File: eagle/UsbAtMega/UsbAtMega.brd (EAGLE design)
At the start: 33.5 x 28.6 mm, 16 parts, among them U1 ATMEGA328P_PDIP, U2 FT232RLSSOP

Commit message: tweaks
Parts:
- added JP1: (no value), SparkFun-Connectors:1X06
- moved Y1 63.5 mm to (60.5, 8.45)
- moved C5 61.1 mm to (52.6, 8.12)
- moved U1 44.8 mm to (55.6, 18.5)
- moved R11 41.0 mm to (38.4, 5.85), turned to 270 degrees
- moved C4 38.9 mm to (32.8, 8.78)
- moved R3 13.9 mm to (30.2, 20.5)
- moved RX 6.70 mm to (24.4, 26.0), turned to 90 degrees
- moved TX 5.81 mm to (16.6, 26.0), turned to 90 degrees
- moved R2 4.97 mm to (11.1, 23.7)
- moved R1 4.65 mm to (7.15, 23.7)
- moved U2 3.91 mm to (19.8, 13.3)
- moved PWR 3.71 mm to (28.6, 5.20), turned to 90 degrees
- moved C2 3.71 mm to (13.3, 5.53), turned to 270 degrees
- moved C3 3.71 mm to (21.1, 3.25)
- moved USB 2.62 mm to (2.60, 17.2)
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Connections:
- removed net 5V1: C5.1
- new net N$10: JP1.5, U1.27
- new net N$11: JP1.4, U1.26
- new net N$12: JP1.3, U1.25
- new net N$18: JP1.2, U1.24
- new net N$19: JP1.1, U1.23
- new net N$9: JP1.6, U1.28
- net 5V: now also C5.1
- net N$1: now also U1.1
- net N$7: now also U1.9
- net N$8: now also U1.10
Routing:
- net 5V: track 77.7 -> 0.00 mm, vias 1 -> 0
- net GND: track 76.2 -> 0.00 mm, vias 1 -> 0
- net 3.3V: track 33.2 -> 0.00 mm, vias 1 -> 0
- net N$13: track 19.8 -> 0.00 mm, vias 1 -> 0
- net N$17: track 17.9 -> 0.00 mm, vias 1 -> 0
- net N$2: track 17.7 -> 0.00 mm
- net N$16: track 15.7 -> 0.00 mm
- net N$14: track 14.9 -> 0.00 mm, vias 1 -> 0
- net N$15: track 13.7 -> 0.00 mm
- net N$3: track 10.5 -> 0.00 mm
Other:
- board size 33.5 x 28.6 mm -> 75.4 x 29.9 mm
- board text removed: "3.3V"
- board text removed: "5V"
- board text removed: "MARKY'S HOUSE"
- board text removed: "USB THANG"

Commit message: Start Manual routing
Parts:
- moved USB 0.32 mm to (2.60, 17.6)
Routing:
- net GND: track 0.00 -> 50.8 mm, vias 0 -> 6
- net 5V: track 0.00 -> 37.3 mm, vias 0 -> 1
- net N$2: track 0.00 -> 21.0 mm, vias 0 -> 1
- net 3.3V: track 0.00 -> 17.6 mm, vias 0 -> 1
- net N$13: track 0.00 -> 16.6 mm, vias 0 -> 1
- net N$3: track 0.00 -> 13.4 mm
- net N$14: track 0.00 -> 12.0 mm, vias 0 -> 1
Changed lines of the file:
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@@
 </autorouter>
 <elements>
-<element name="USB" library="SparkFun-Connectors" package="1X04_LOCK" value="" x="2.6" y="17.225" smashed="yes" rot="R270">
-<attribute name="NAME" x="0.8538" y="18.8962" size="1.27" layer="25" ratio="10"/>
-<attribute name="VALUE" x="-0.575" y="18.495" size="1.27" layer="27" rot="R270"/>
+<element name="USB" library="SparkFun-Connectors" package="1X04_LOCK" value="" x="2.6" y="17.55" smashed="yes" rot="R270">
+<attribute name="NAME" x="0.8538" y="19.2212" size="1.27" layer="25" ratio="10"/>
+<attribute name="VALUE" x="-0.575" y="18.82" size="1.27" layer="27" rot="R270"/>
 </element>
 <element name="U2" library="SparkFun-DigitalIC" package="SSOP28DB" value="FT232RLSSOP" x="19.825" y="13.325" smashed="yes" rot="R90">
 <attribute name="PROD_ID" value="IC-00870" x="19.825" y="13.325" size="1.778" layer="27" rot="R90" display="off"/>
-<attribute name="NAME" x="17.905" y="8.54" size="0.4064" layer="25" rot="R90"/>
+<attribute name="NAME" x="18.23" y="8.865" size="0.4064" layer="25" rot="R90"/>
 </element>
 <element name="C1" library="SparkFun-Capacitors" package="CAP-PTH-SMALLEZ" value="0.1uF" x="7.15" y="4.225" smashed="yes" rot="R90">
@@
 <contactref element="USB" pad="4"/>
 <contactref element="U2" pad="16"/>
-<wire x1="2.473" y1="9.605" x2="16.169" y2="16.9" width="0" layer="19" extent="1-1"/>
+<wire x1="16.169" y1="16.9" x2="5.85" y2="16.9" width="0.4064" layer="1"/>
+<wire x1="5.85" y1="16.9" x2="5.85" y2="16.25" width="0.4064" layer="1"/>
+<wire x1="5.85" y1="16.25" x2="4.55" y2="16.25" width="0.4064" layer="1"/>
+<via x="4.55" y="16.25" extent="1-16" drill="0.6"/>
+<wire x1="4.55" y1="16.25" x2="4.55" y2="9.75" width="0.4064" layer="16"/>
+<wire x1="4.55" y1="9.75" x2="2.473" y2="9.75" width="0.4064" layer="16"/>
+<wire x1="2.473" y1="9.75" x2="2.473" y2="9.93" width="0.4064" layer="16"/>
 </signal>
 <signal name="N$3">
 <contactref element="USB" pad="1"/>
 <contactref element="U2" pad="15"/>
-<wire x1="2.727" y1="17.225" x2="16.169" y2="17.55" width="0" layer="19" extent="1-1"/>
+<wire x1="16.169" y1="17.55" x2="2.727" y2="17.55" width="0.4064" layer="1"/>
 </signal>
 <signal name="GND">
@@
 <contactref element="U1" pad="22"/>
 <contactref element="C5" pad="2"/>
+<wire x1="2.473" y1="15.01" x2="6.115" y2="15.01" width="0.4064" layer="1"/>
+<wire x1="6.115" y1="15.01" x2="6.175" y2="14.95" width="0.4064" layer="1"/>
+<via x="6.175" y="14.95" extent="1-16" drill="0.6"/>
+<wire x1="6.175" y1="14.95" x2="6.175" y2="7.74" width="0.4064" layer="16"/>
+<wire x1="6.175" y1="7.74" x2="7.15" y2="6.765" width="0.4064" layer="16"/>
+<wire x1="7.15" y1="6.765" x2="13.295" y2="6.765" width="0.4064" layer="1"/>
+<wire x1="13.295" y1="6.765" x2="13.325" y2="6.795" width="0.4064" layer="1"/>
+<wire x1="13.325" y1="6.795" x2="18.495" y2="6.795" width="0.4064" layer="1"/>
+<wire x1="18.495" y1="6.795" x2="18.525" y2="6.825" width="0.4064" layer="1"/>
+<via x="18.525" y="6.825" extent="1-16" drill="0.6"/>
+<wire x1="18.585" y1="3.25" x2="18.585" y2="6.765" width="0.4064" layer="16"/>
+<wire x1="18.585" y1="6.765" x2="18.525" y2="6.825" width="0.4064" layer="16"/>
+<wire x1="16.169" y1="10.4" x2="18.525" y2="10.4" width="0.4064" layer="1"/>
+<wire x1="16.169" y1="11.05" x2="17.875" y2="11.05" width="0.4064" layer="1"/>
+<wire x1="17.875" y1="11.05" x2="18.525" y2="11.7" width="0.4064" layer="1"/>
+<via x="18.525" y="10.4" extent="1-16" drill="0.6"/>
+<via x="18.525" y="11.7" extent="1-16" drill="0.6"/>
+<wire x1="18.525" y1="10.4" x2="18.525" y2="6.825" width="0.4064" layer="16"/>
+<wire x1="18.525" y1="11.7" x2="18.525" y2="10.4" width="0.4064" layer="16"/>
+<wire x1="23.481" y1="13" x2="19.175" y2="13" width="0.4064" layer="1"/>
+<wire x1="19.175" y1="13" x2="18.525" y2="13.65" width="0.4064" layer="1"/>
+<via x="18.525" y="13.65" extent="1-16" drill="0.6"/>
+<wire x1="18.525" y1="11.7" x2="18.525" y2="13.65" width="0.4064" layer="16"/>
+<wire x1="16.169" y1="13.65" x2="18.525" y2="13.65" width="0.4064" layer="1"/>
 <wire x1="56.845" y1="14.715" x2="54.305" y2="22.335" width="0" layer="19" extent="1-1"/>
 <wire x1="55.19" y1="8.125" x2="56.845" y2="14.715" width="0" layer="19" extent="1-1"/>
-<wire x1="23.481" y1="13" x2="54.305" y2="22.335" width="0" layer="19" extent="1-1"/>
-<wire x1="16.169" y1="13.65" x2="23.481" y2="13" width="0" layer="19" extent="1-1"/>
-<wire x1="16.169" y1="15.6" x2="16.169" y2="13.65" width="0" layer="19" extent="1-1"/>
-<wire x1="16.169" y1="11.05" x2="16.169" y2="13.65" width="0" layer="19" extent="1-1"/>
-<wire x1="16.169" y1="10.4" x2="16.169" y2="11.05" width="0" layer="19" extent="1-1"/>
-<wire x1="13.325" y1="6.795" x2="16.169" y2="10.4" width="0" layer="19" extent="1-1"/>
-<wire x1="18.585" y1="3.25" x2="13.325" y2="6.795" width="0" layer="19" extent="1-1"/>
-<wire x1="26.415" y1="20.475" x2="16.169" y2="15.6" width="0" layer="19" extent="1-1"/>
-<wire x1="7.15" y1="6.765" x2="13.325" y2="6.795" width="0" layer="19" extent="1-1"/>
-<wire x1="2.473" y1="14.685" x2="7.15" y2="6.765" width="0" layer="19" extent="1-1"/>
+<wire x1="26.415" y1="20.475" x2="54.305" y2="22.335" width="0" layer="19" extent="1-1"/>
+<wire x1="23.481" y1="13" x2="26.415" y2="20.475" width="0" layer="19" extent="1-1"/>
+<wire x1="16.169" y1="15.6" x2="18.2" y2="15.6" width="0.4064" layer="1"/>
+<wire x1="18.2" y1="15.6" x2="18.525" y2="15.275" width="0.4064" layer="1"/>
+<via x="18.525" y="15.275" extent="1-16" drill="0.6"/>
+<wire x1="18.525" y1="15.275" x2="18.525" y2="13.65" width="0.4064" layer="16"/>
 </signal>
 <signal name="3.3V">
 <contactref element="C3" pad="1"/>
 <contactref element="U2" pad="17"/>
-<wire x1="21.125" y1="3.25" x2="16.169" y2="16.25" width="0" layer="19" extent="1-1"/>
+<wire x1="21.125" y1="3.25" x2="20.475" y2="3.9" width="0.4064" layer="16"/>
+<wire x1="20.475" y1="3.9" x2="20.475" y2="16.25" width="0.4064" layer="16"/>
+<via x="20.475" y="16.25" extent="1-16" drill="0.6"/>
+<wire x1="20.475" y1="16.25" x2="16.169" y2="16.25" width="0.4064" layer="1"/>
 </signal>
 <signal name="5V">
@@
 <contactref element="U1" pad="21"/>
 <contactref element="C5" pad="1"/>
+<wire x1="7.15" y1="4.225" x2="5.2" y2="4.225" width="0.4064" layer="16"/>
+<wire x1="5.2" y1="4.225" x2="0.975" y2="8.45" width="0.4064" layer="16"/>
+<wire x1="0.975" y1="8.45" x2="0.975" y2="10.718" width="0.4064" layer="16"/>
+<wire x1="0.975" y1="10.718" x2="2.727" y2="12.47" width="0.4064" layer="16"/>
 <wire x1="56.845" y1="22.335" x2="59.385" y2="22.335" width="0" layer="19" extent="1-1"/>
 <wire x1="54.305" y1="14.715" x2="56.845" y2="22.335" width="0" layer="19" extent="1-1"/>
@@
 <wire x1="28.6" y1="3.93" x2="38.35" y2="2.04" width="0" layer="19" extent="1-1"/>
 <wire x1="23.481" y1="11.05" x2="28.6" y2="3.93" width="0" layer="19" extent="1-1"/>
+<wire x1="24.375" y1="24.73" x2="16.575" y2="24.73" width="0" layer="19" extent="1-1"/>
+<wire x1="7.15" y1="4.225" x2="13.295" y2="4.225" width="0.4064" layer="1"/>
+<wire x1="13.295" y1="4.225" x2="13.325" y2="4.255" width="0.4064" layer="1"/>
+<wire x1="13.325" y1="4.255" x2="13.295" y2="4.255" width="0.4064" layer="16"/>
+<wire x1="13.295" y1="4.255" x2="9.425" y2="8.125" width="0.4064" layer="16"/>
+<wire x1="9.425" y1="8.125" x2="9.425" y2="14.3" width="0.4064" layer="16"/>
+<via x="9.425" y="14.3" extent="1-16" drill="0.6"/>
+<wire x1="9.425" y1="14.3" x2="16.169" y2="14.3" width="0.4064" layer="1"/>
+<wire x1="16.575" y1="24.73" x2="16.169" y2="14.3" width="0" layer="19" extent="1-1"/>
 <wire x1="16.169" y1="14.3" x2="23.481" y2="11.05" width="0" layer="19" extent="1-1"/>
-<wire x1="13.325" y1="4.255" x2="16.169" y2="14.3" width="0" layer="19" extent="1-1"/>
-<wire x1="7.15" y1="4.225" x2="13.325" y2="4.255" width="0" layer="19" extent="1-1"/>
-<wire x1="2.727" y1="12.145" x2="13.325" y2="4.255" width="0" layer="19" extent="1-1"/>
-<wire x1="24.375" y1="24.73" x2="16.169" y2="14.3" width="0" layer="19" extent="1-1"/>
-<wire x1="16.575" y1="24.73" x2="24.375" y2="24.73" width="0" layer="19" extent="1-1"/>
 </signal>
 <signal name="N$13">
 <contactref element="U2" pad="23"/>
 <contactref element="R1" pad="P$1"/>
-<wire x1="7.15" y1="19.915" x2="16.169" y2="12.35" width="0" layer="19" extent="1-1"/>
+<wire x1="7.15" y1="19.915" x2="7.15" y2="12.35" width="0.4064" layer="16"/>
+<via x="7.15" y="12.35" extent="1-16" drill="0.6"/>
+<wire x1="16.169" y1="12.35" x2="7.15" y2="12.35" width="0.4064" layer="1"/>
 </signal>
 <signal name="N$14">
 <contactref element="U2" pad="22"/>
 <contactref element="R2" pad="P$1"/>
-<wire x1="16.169" y1="13" x2="11.05" y2="19.915" width="0" layer="19" extent="1-1"/>
+<wire x1="11.05" y1="19.915" x2="11.375" y2="19.915" width="0.4064" layer="16"/>
+<wire x1="11.375" y1="19.915" x2="11.375" y2="13.325" width="0.4064" layer="16"/>
+<via x="11.375" y="13.325" extent="1-16" drill="0.6"/>
+<wire x1="16.169" y1="13" x2="13.65" y2="13" width="0.4064" layer="1"/>
+<wire x1="13.65" y1="13" x2="13.65" y2="13.325" width="0.4064" layer="1"/>
+<wire x1="13.65" y1="13.325" x2="11.375" y2="13.325" width="0.4064" layer="1"/>
 </signal>
 <signal name="N$15">

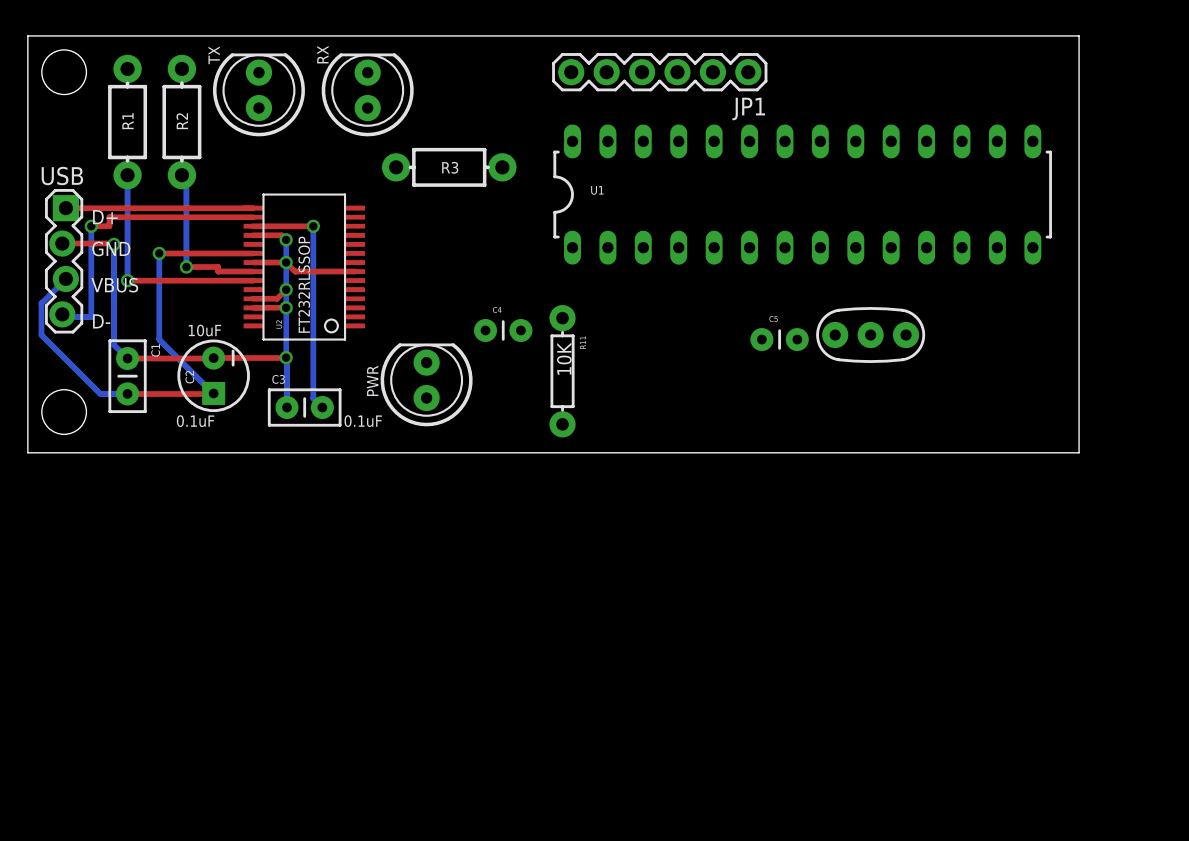
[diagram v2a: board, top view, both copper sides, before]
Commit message: Finish manual routing for USB <--> AtMega
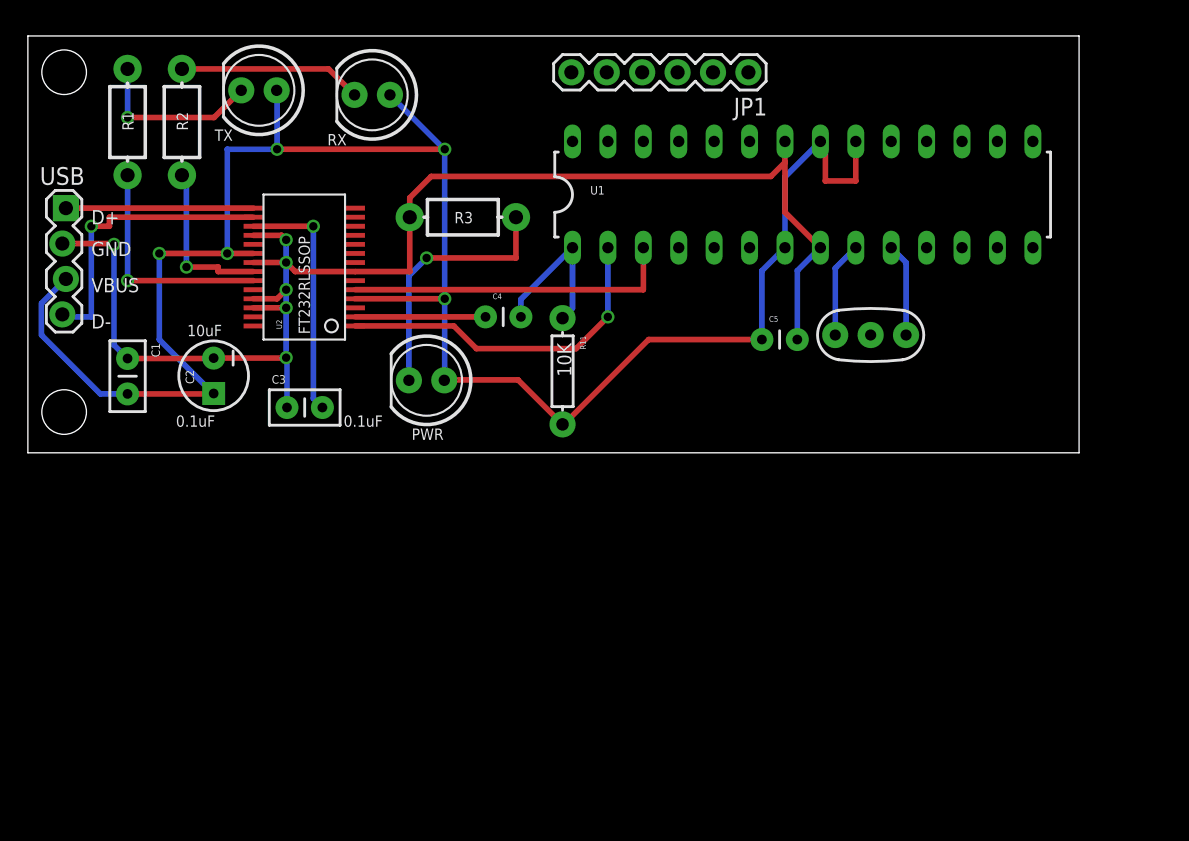
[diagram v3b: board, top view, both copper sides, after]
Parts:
- moved R3 3.71 mm to (31.2, 16.9)
- moved C4 0.97 mm to (32.8, 9.75)
- moved RX 0.46 mm to (24.7, 25.7), turned to 180 degrees
- turned PWR to 180 degrees
- turned TX to 180 degrees
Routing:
- net 5V: track 37.3 -> 143.9 mm, vias 1 -> 6
- net GND: track 50.8 -> 103.9 mm
- net N$5: track 0.00 -> 24.7 mm, vias 0 -> 1
- net N$6: track 0.00 -> 23.7 mm
- net N$17: track 0.00 -> 18.6 mm, vias 0 -> 1
- net N$16: track 0.00 -> 13.2 mm
- net N$15: track 0.00 -> 12.4 mm, vias 0 -> 1
- net N$1: track 0.00 -> 11.8 mm
- net N$4: track 0.00 -> 9.34 mm
- net N$7: track 0.00 -> 6.88 mm
- net N$8: track 0.00 -> 6.71 mm

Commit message: Experiments repositioning AtMega to try to get something shield-able.
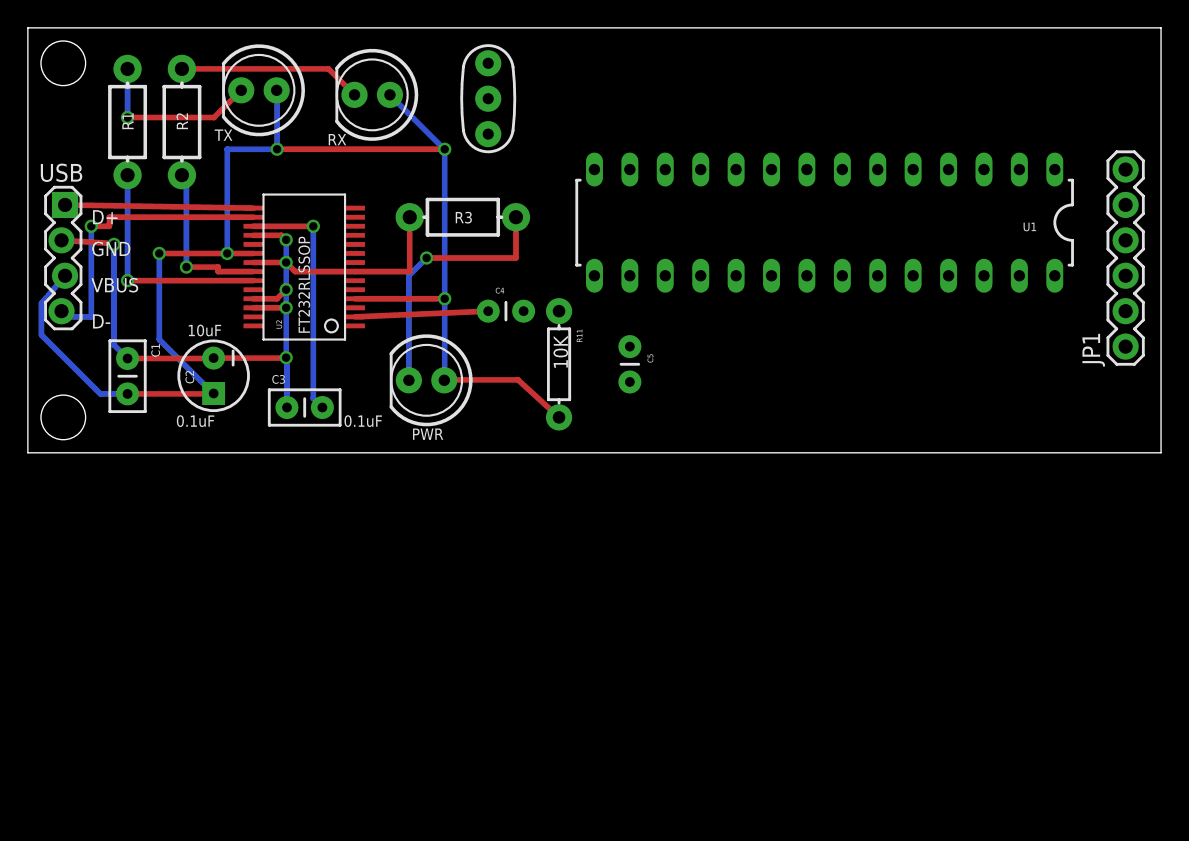
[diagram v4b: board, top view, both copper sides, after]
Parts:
- moved JP1 33.5 mm to (78.7, 7.62), turned to 90 degrees
- moved Y1 32.2 mm to (33.0, 25.4), turned to 270 degrees
- moved C5 9.48 mm to (43.2, 7.62), turned to 270 degrees
- moved U1 2.56 mm to (57.1, 16.5), turned to 180 degrees
- moved R11 0.56 mm to (38.1, 6.35)
- moved C4 0.45 mm to (33.0, 10.2)
- moved USB 0.24 mm to (2.54, 17.8)
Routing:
- net GND: track 103.9 -> 58.7 mm
- net 5V: track 143.9 -> 102.5 mm
- net N$5: track 24.7 -> 0.00 mm, vias 1 -> 0
- net N$6: track 23.7 -> 0.00 mm
- net N$1: track 11.8 -> 0.00 mm
- net N$7: track 6.88 -> 0.00 mm
- net N$8: track 6.71 -> 0.00 mm
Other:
- board size 75.4 x 29.9 mm -> 81.3 x 30.5 mm
